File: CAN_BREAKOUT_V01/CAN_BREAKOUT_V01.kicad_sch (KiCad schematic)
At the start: 63 parts, among them J1 Conn_01x04, J2 Conn_01x04, J3 Conn_01x04, J4 Conn_01x04, J5 Conn_01x04, J6 Conn_01x04, J7 Conn_01x04, J8 Conn_01x04, Q1 PMOS, U1 LE33CZ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

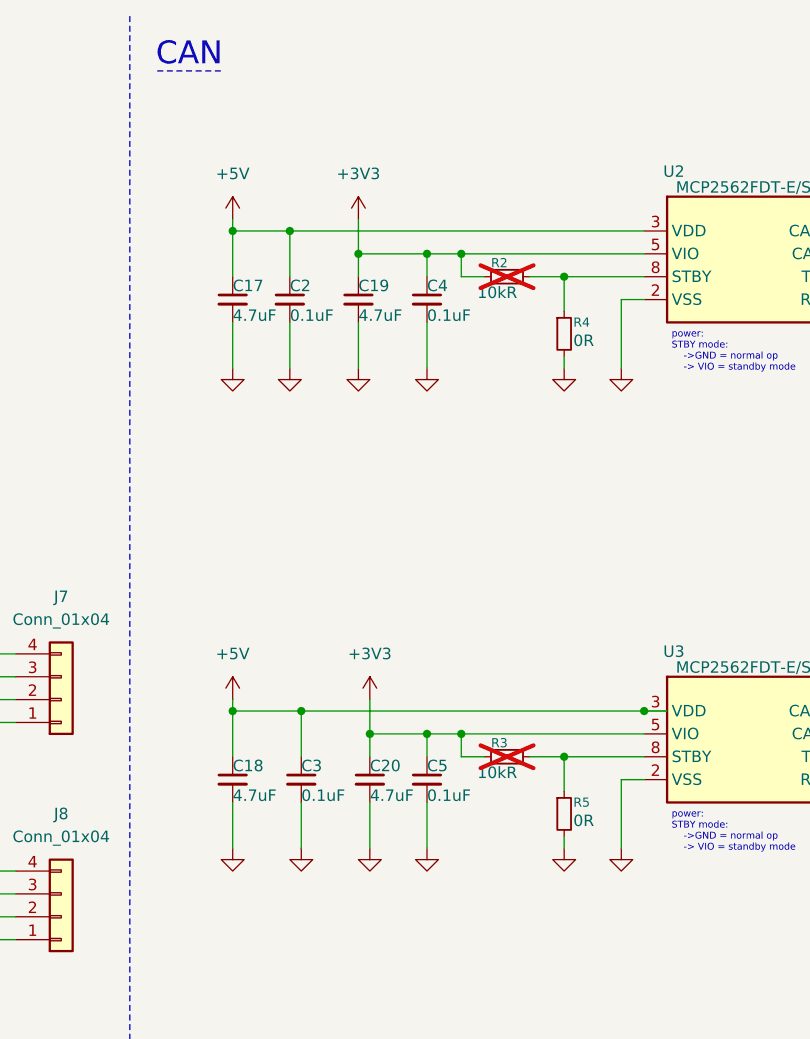
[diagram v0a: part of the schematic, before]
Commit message: updated to break out SYNC pin to enable MCU control of redundancy channel; still getting text warnings, dont know how to change rules yet..
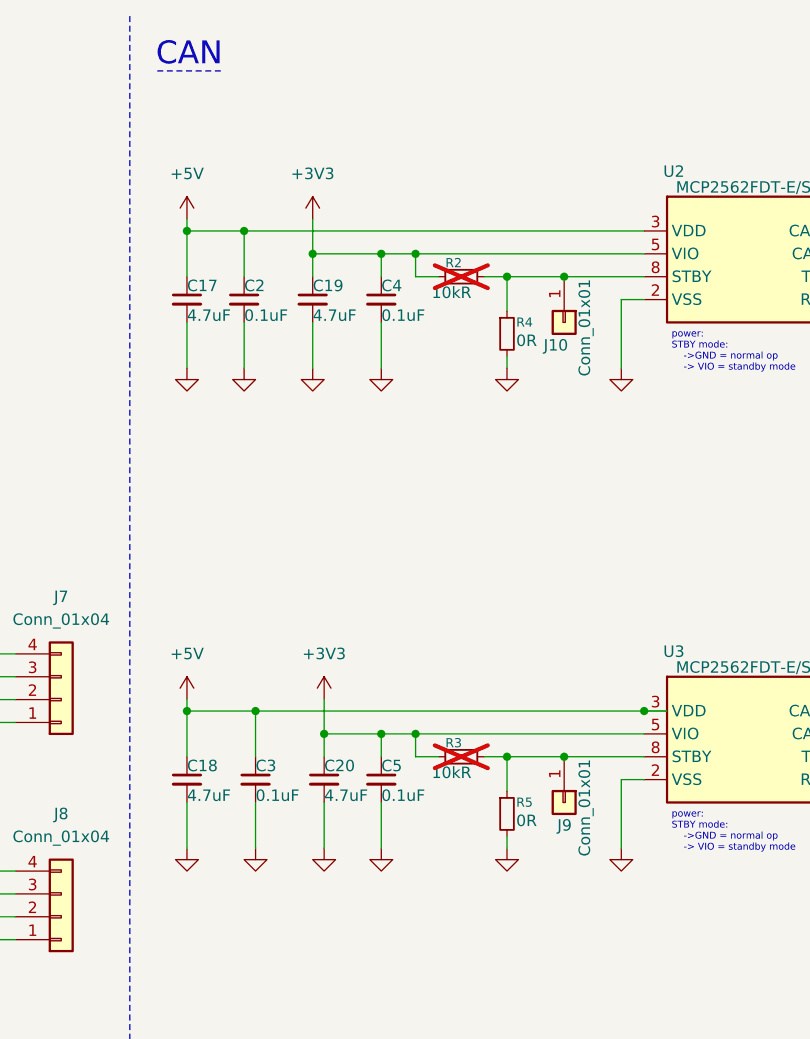
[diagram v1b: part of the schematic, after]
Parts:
- added J10, J9: Conn_01x01, Connector_PinHeader_2.54mm:PinHeader_1x01_P2.54mm_Vertical, symbol Connector_Generic:Conn_01x01
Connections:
- net at R3.1, R5.1, U3.8 (STBY): now also J9.1 (Pin_1)
- net at R2.1, R4.1, U2.8 (STBY): now also J10.1 (Pin_1)
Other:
- moved on the sheet: C17, C18, C19, C2, C20, C3, C4, C5, R2, R3, R4, R5
